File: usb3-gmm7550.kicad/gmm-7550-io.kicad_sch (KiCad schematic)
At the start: 25 parts

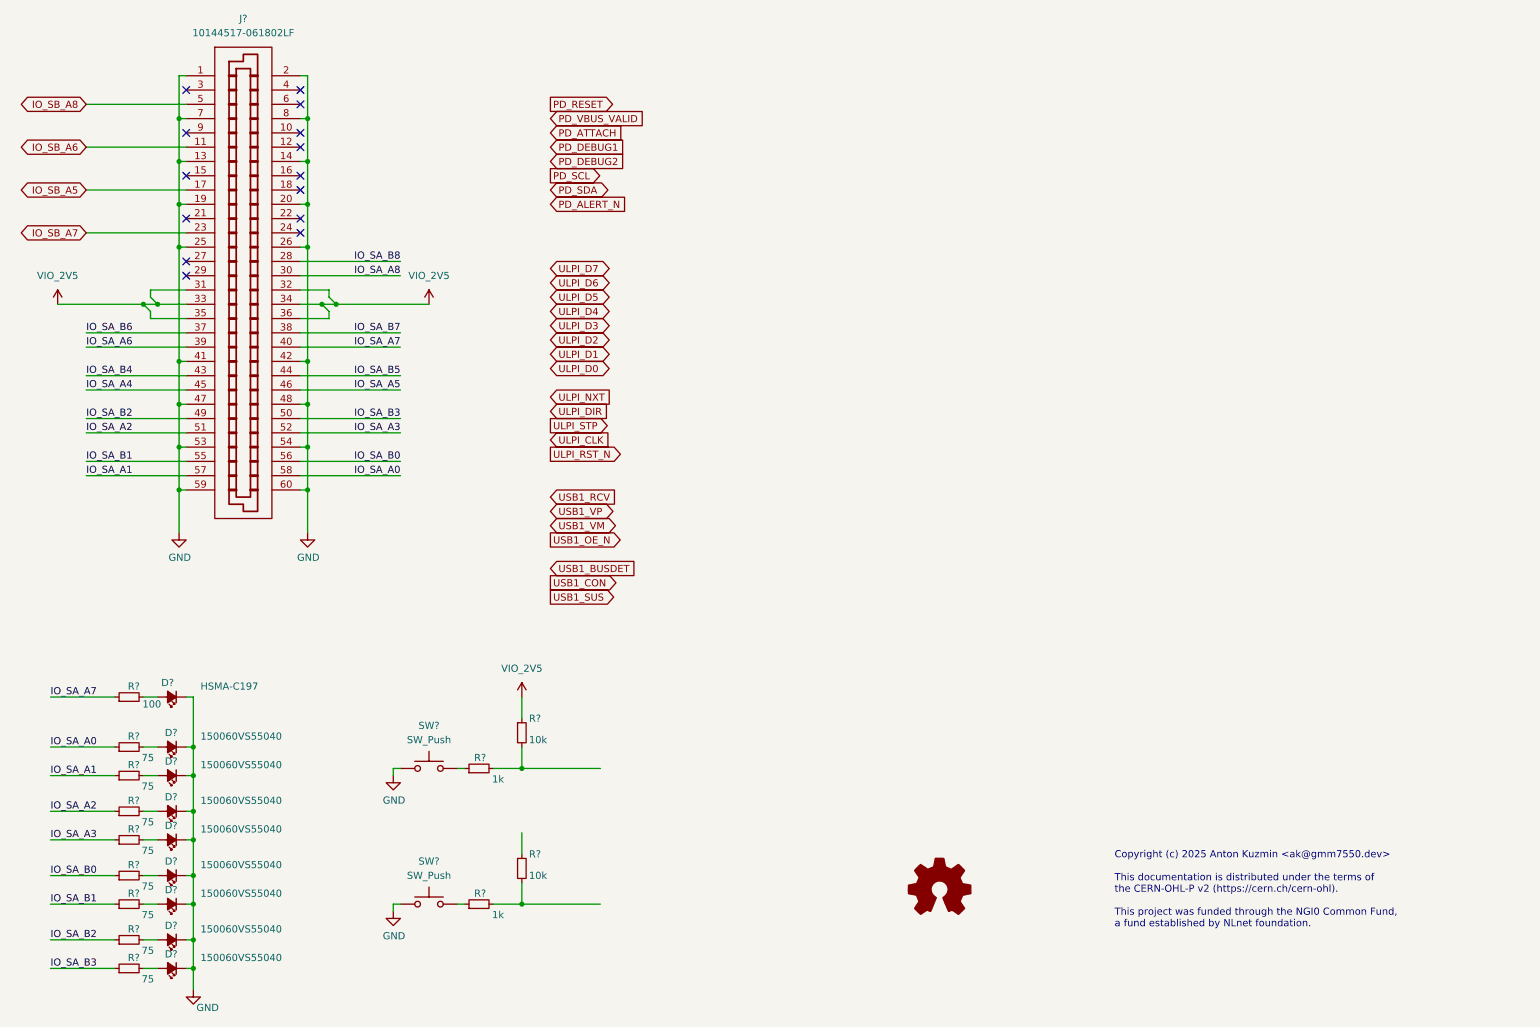
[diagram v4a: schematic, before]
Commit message: USB 3 adapter schematic: revision 0.9 (pre-layout) is ready
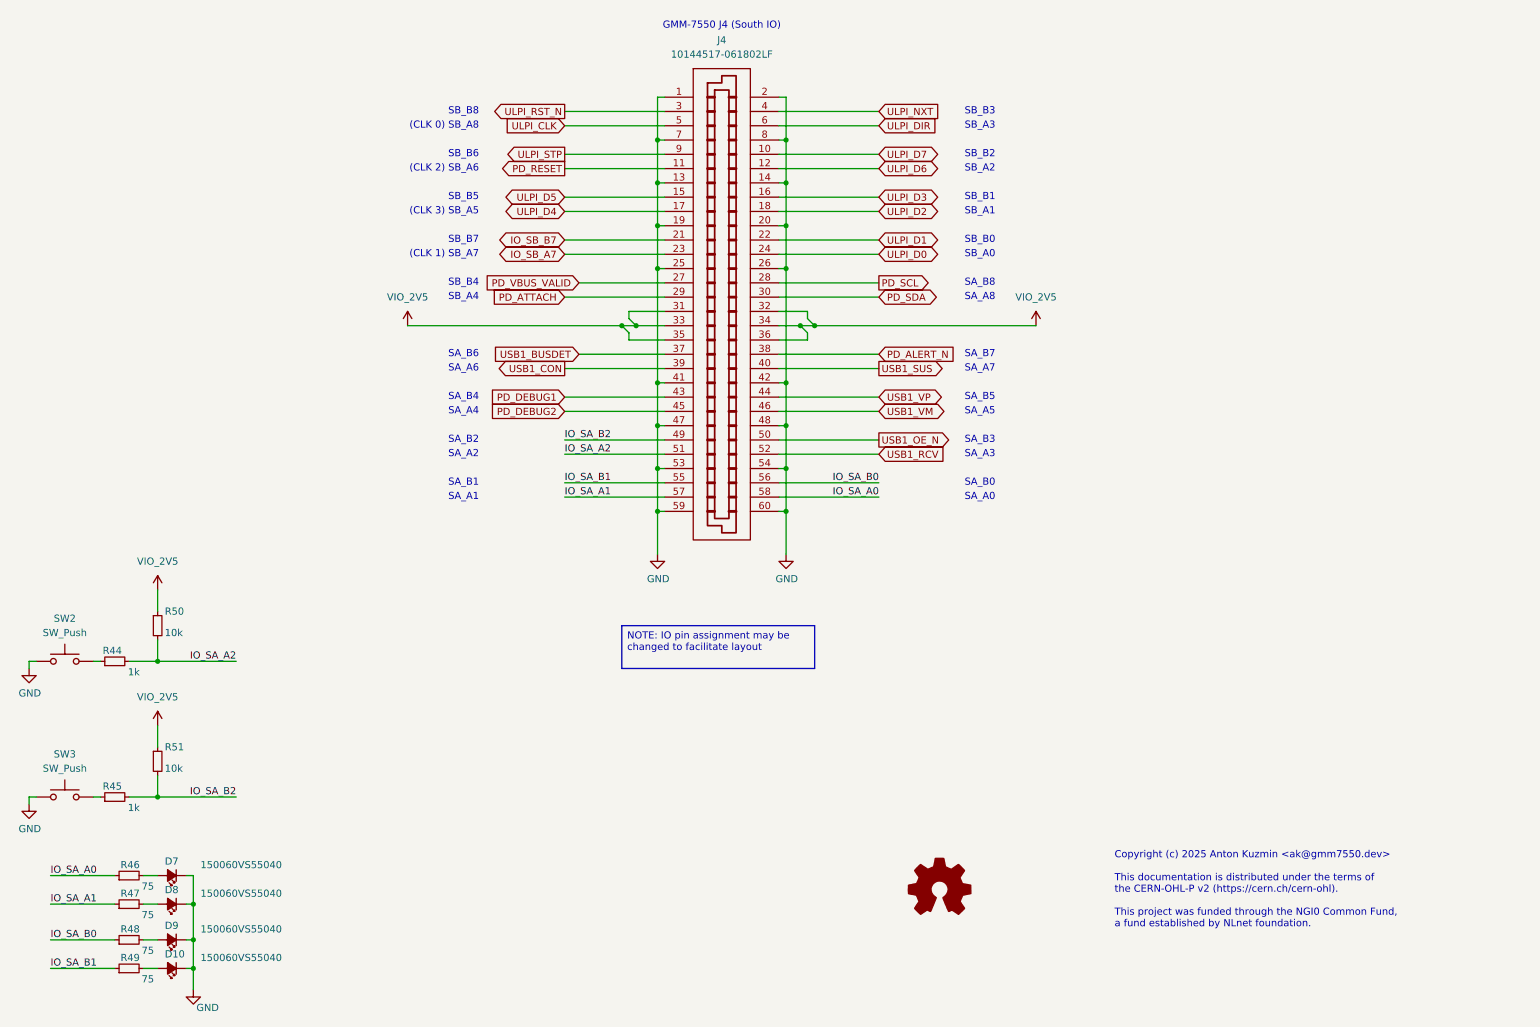
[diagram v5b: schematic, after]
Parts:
- removed D? (x4): 150060VS55040, LED_SMD:LED_0603_1608Metric, symbol Device:LED_Small_Filled
- removed D?: HSMA-C197, LED_SMD:LED_0603_1608Metric, symbol Device:LED_Small_Filled
- removed R?: 100, Resistor_SMD:R_0603_1608Metric, symbol Device:R_Small
- removed R? (x4): 75, Resistor_SMD:R_0603_1608Metric, symbol Device:R_Small
- gave numbers to parts that had none: 15
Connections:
- net IO_SA_A3 is gone; now on net USB1_RCV: J4.52
- net IO_SA_A4 is gone; now on net PD_DEBUG2: J4.45
- net IO_SA_A5 is gone; now on net USB1_VM: J4.46
- net IO_SA_A6 is gone; now on net USB1_CON: J4.39
- net IO_SA_A7 is gone; now on net USB1_SUS: J4.40
- net IO_SA_A8 is gone; now on net PD_SDA: J4.30
- net IO_SA_B3 is gone; now on net USB1_OE_N: J4.50
- net IO_SA_B4 is gone; now on net PD_DEBUG1: J4.43
- net IO_SA_B5 is gone; now on net USB1_VP: J4.44
- net IO_SA_B6 is gone; now on net USB1_BUSDET: J4.37
- net IO_SA_B7 is gone; now on net PD_ALERT_N: J4.38
- net IO_SA_B8 is gone; now on net PD_SCL: J4.28
- net IO_SB_A5 is gone; now on net ULPI_D4: J4.17
- net IO_SB_A6 is gone; now on net PD_RESET: J4.11
- net IO_SB_A8 is gone; now on net ULPI_CLK: J4.5
- net IO_SA_A2: now also R44.2, R50.2
- net IO_SA_B2: now also R45.2, R51.2
- net PD_ATTACH: now also J4.29
- net PD_VBUS_VALID: now also J4.27
- net ULPI_D0: now also J4.24
- net ULPI_D1: now also J4.22
- net ULPI_D2: now also J4.18
- net ULPI_D3: now also J4.16
- net ULPI_D5: now also J4.15
- net ULPI_D6: now also J4.12
- net ULPI_D7: now also J4.10
- net ULPI_DIR: now also J4.6
- net ULPI_NXT: now also J4.4
- net ULPI_RST_N: now also J4.3
- net ULPI_STP: now also J4.9
- net VIO_2V5: now also R51.1
- net IO_SB_B7: now reaches J4.21
- no-connect marks 14 -> 0
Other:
- note added: "(CLK 0) SB_A8"
- note added: "(CLK 1) SB_A7"
- note added: "(CLK 2) SB_A6"
- note added: "(CLK 3) SB_A5"
- note added: "GMM-7550 J4 (South IO)"
- note added: "SA_A0"
- note added: "SA_A1"
- note added: "SA_A2"
- note added: "SA_A3"
- note added: "SA_A4"
- note added: "SA_A5"
- note added: "SA_A6"
- note added: "SA_A7"
- note added: "SA_A8"
- note added: "SA_B0"
- note added: "SA_B1"
- note added: "SA_B2"
- note added: "SA_B3"
- note added: "SA_B4"
- note added: "SA_B5"
- note added: "SA_B6"
- note added: "SA_B7"
- note added: "SA_B8"
- note added: "SB_A0"
- note added: "SB_A1"
- note added: "SB_A2"
- note added: "SB_A3"
- note added: "SB_A4"
- note added: "SB_B0"
- note added: "SB_B1"
- note added: "SB_B2"
- note added: "SB_B3"
- note added: "SB_B4"
- note added: "SB_B5"
- note added: "SB_B6"
- note added: "SB_B7"
- note added: "SB_B8"
- moved on the sheet: D10, D7, D8, D9, J4, R44, R45, R46, R47, R48, R49, R50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

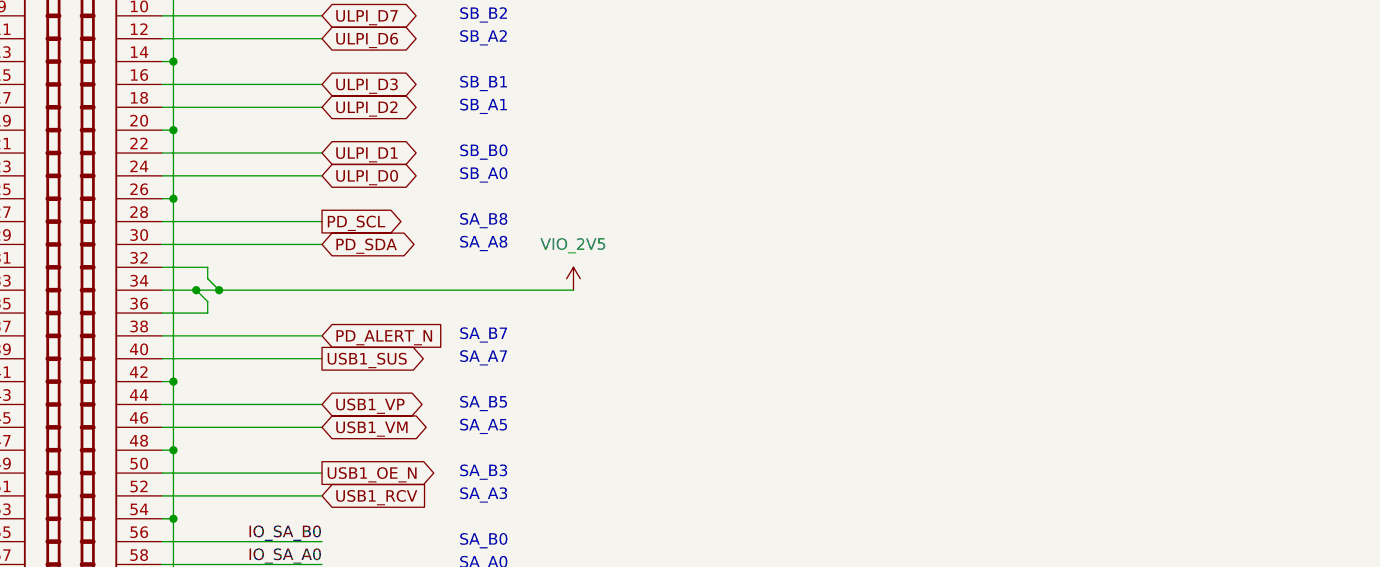
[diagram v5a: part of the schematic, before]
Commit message: Placement: WIP, schematic update to 0.9.1 -- BoM simplification and minor improvements
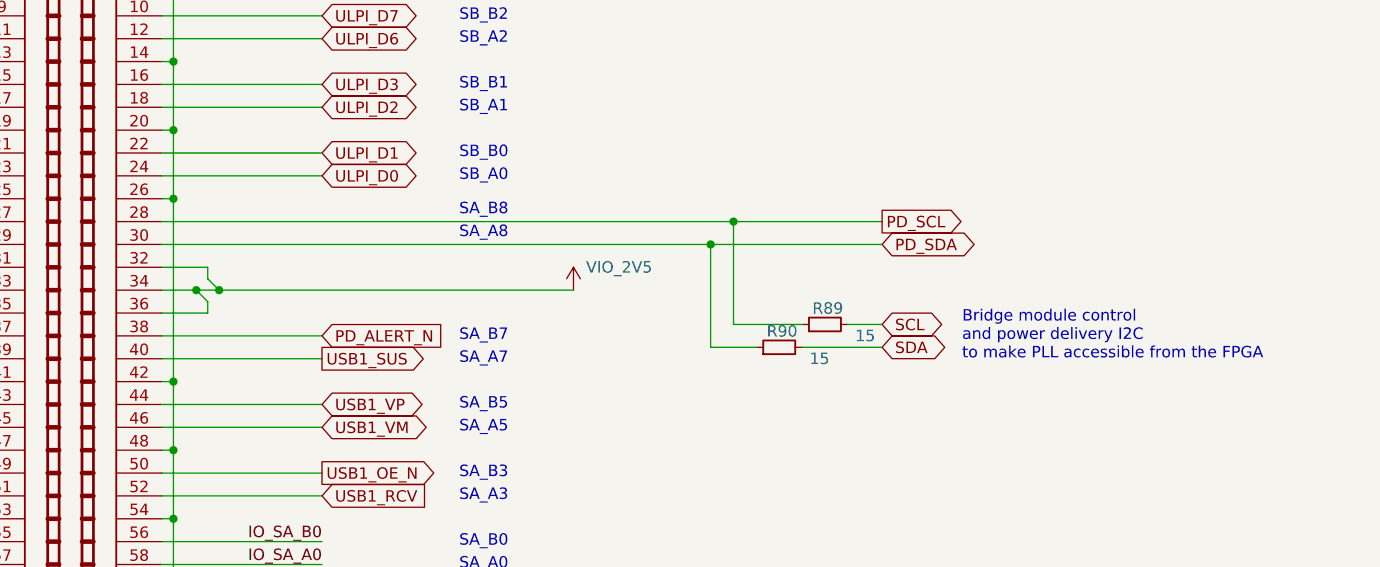
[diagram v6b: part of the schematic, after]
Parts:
- added R89, R90: 15, Resistor_SMD:R_0402_1005Metric, symbol Device:R_Small
- SW2, SW3: footprint pts810:SW_SPST_PTS810 -> Button_Switch_SMD:SW_SPST_PTS810
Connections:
- net PD_SCL: now also R89.1
- net PD_SDA: now also R90.1
- new net SCL: R89.2
- new net SDA: R90.2
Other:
- note added: "Bridge module control and power delivery I2C to make PLL accessible from the FPGA"

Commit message: Change to smaller resistors
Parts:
- R46, R47, R48, R49: footprint Resistor_SMD:R_0603_1608Metric -> Resistor_SMD:R_0402_1005Metric
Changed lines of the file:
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@@
 			)
 		)
-		(property "Footprint" "Resistor_SMD:R_0603_1608Metric"
+		(property "Footprint" "Resistor_SMD:R_0402_1005Metric"
 			(at 39.37 182.88 0)
 			(effects
@@
 			)
 		)
-		(property "Footprint" "Resistor_SMD:R_0603_1608Metric"
+		(property "Footprint" "Resistor_SMD:R_0402_1005Metric"
 			(at 39.37 187.96 0)
 			(effects
@@
 			)
 		)
-		(property "Footprint" "Resistor_SMD:R_0603_1608Metric"
+		(property "Footprint" "Resistor_SMD:R_0402_1005Metric"
 			(at 39.37 176.53 0)
 			(effects
@@
 			)
 		)
-		(property "Footprint" "Resistor_SMD:R_0603_1608Metric"
+		(property "Footprint" "Resistor_SMD:R_0402_1005Metric"
 			(at 39.37 171.45 0)
 			(effects
